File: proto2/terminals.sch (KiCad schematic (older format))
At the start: 111 parts, among them J1 Output 1, J10 Output 6, J11 Device 4, J2 Main Power, J3 Output 2, J4 Output 3, J5 Device 4, J6 Output 4, J7 Device 4, J8 Output 5, J9 Device 4

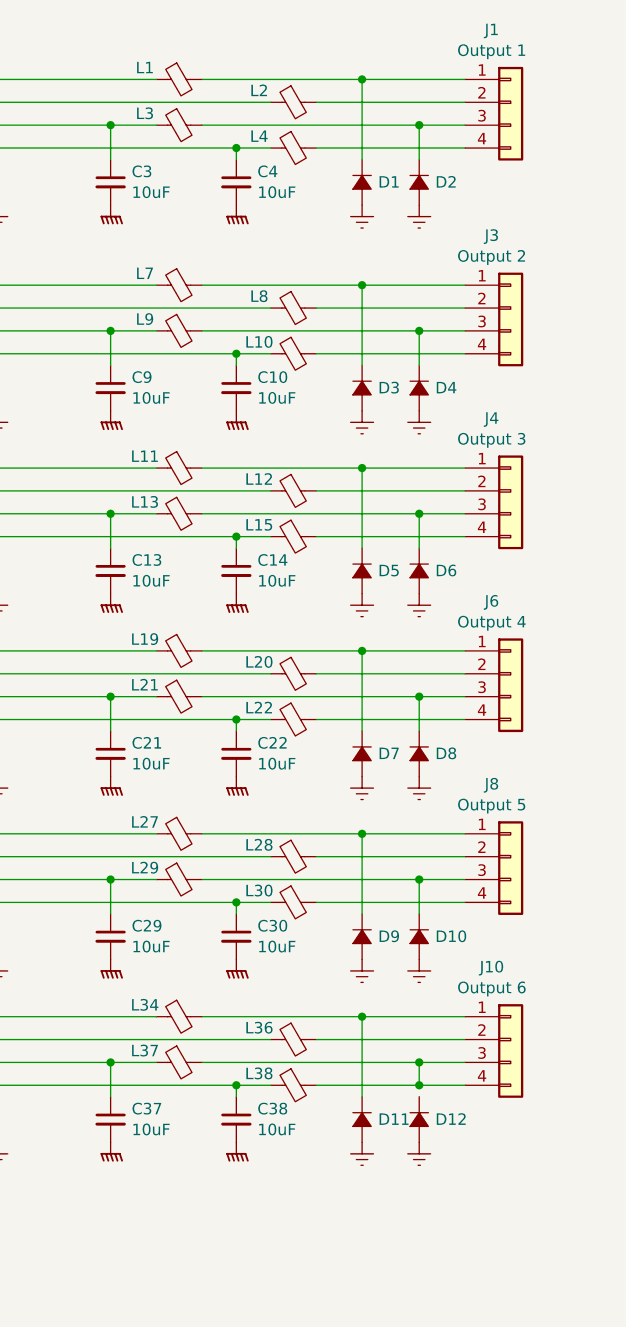
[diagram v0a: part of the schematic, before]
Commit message: Routed Board.
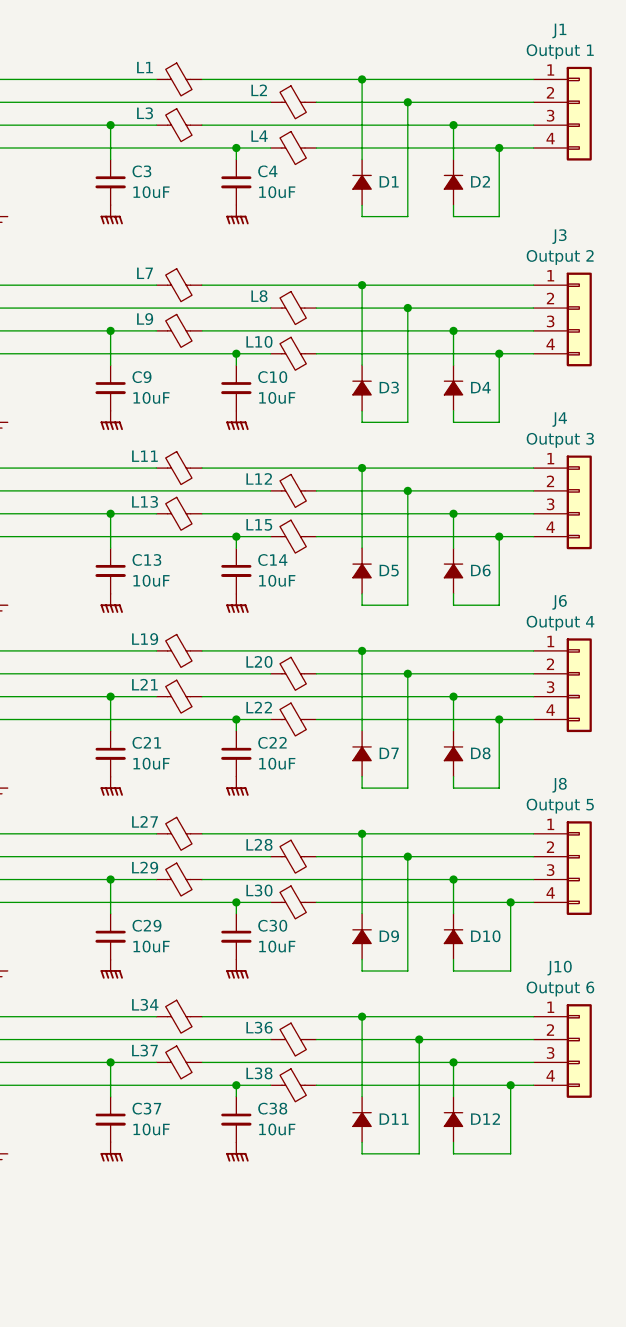
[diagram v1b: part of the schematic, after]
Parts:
- L5, L6: footprint Resistor_SMD:R_1206_3216Metric -> Inductor_BCR:Coilmax_MS0630-2R2M
- MH1, MH2, MH3, MH4: footprint BCR_STD:STD-M6 -> STD-xxx:STD-.125_wide
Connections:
- net Earth: no longer D1.2 (A), D10.2 (A), D11.2 (A), D12.2 (A), D2.2 (A), D3.2 (A), D4.2 (A), D5.2 (A), D6.2 (A), D7.2 (A), D8.2 (A), D9.2 (A)
- net at J1.2 (Pin_2), L2.2: now also D1.2 (A)
- net at J1.4 (Pin_4), L4.2: now also D2.2 (A)
- net at J3.2 (Pin_2), L8.2: now also D3.2 (A)
- net at J3.4 (Pin_4), L10.2: now also D4.2 (A)
- net at J4.2 (Pin_2), L12.2: now also D5.2 (A)
- net at J4.4 (Pin_4), L15.2: now also D6.2 (A)
- net at J6.2 (Pin_2), L20.2: now also D7.2 (A)
- net at J6.4 (Pin_4), L22.2: now also D8.2 (A)
- net at J8.2 (Pin_2), L28.2: now also D9.2 (A)
- net at J8.4 (Pin_4), L30.2: now also D10.2 (A)
- net at J10.2 (Pin_2), L36.2: now also D11.2 (A)
- net at J10.3 (Pin_3), L37.2: now also D12.1 (K); no longer J10.4 (Pin_4), L38.2
- new net: D12.2 (A), J10.4 (Pin_4), L38.2
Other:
- moved on the sheet: D10, D12, D2, D4, D6, D8, J1, J10, J3, J4, J6, J8

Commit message: Finished routing board and other changes, bad commit message, I know.
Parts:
- C1, C10, C11, C12, C13, C14, C15, C16, C17, C18, C19, C2, C20, C21, C22, C23, C24, C25, C26, C27, C28, C29, C3, C30, C31, C32, C33, C34, C35, C36, C37, C38, C39, C4, C40, C41, C42, C7, C8, C9: LCSC (none) -> C440198; LSCS C440198 -> (none)
- C5, C6: LCSC (none) -> C440198
- D1, D10, D11, D12, D2, D3, D4, D5, D6, D7, D8, D9: footprint Diode_SMD:D_0805_2012Metric -> Diode_SMD:D_SOD-123F; LCSC (none) -> C64898; Manufacturer (none) -> MDD; Part Number (none) -> SM4007PL
- J10: value Output 6 -> Output
- J11, J5, J7, J9: value Device 4 -> Device
- J3: value Output 2 -> Output
- J4: value Output 3 -> Output
- J6: value Output 4 -> Output
- J8: value Output 5 -> Output
- L1, L10, L11, L12, L13, L15, L19, L2, L20, L21, L22, L27, L28, L29, L3, L30, L34, L36, L37, L38, L4, L7, L8, L9: value Ferrite_Bead_Small -> 1A Ferrite; LCSC (none) -> C405012
- L14, L16, L17, L18, L23, L24, L25, L26, L31, L32, L33, L35, L39, L40, L41, L42: value Ferrite_Bead_Small -> 500mA Ferrite; LCSC (none) -> C1017
- L5, L6: value 100R 5A -> 100R 5A Ferrite; LCSC (none) -> C380175; Manufacturer (none) -> Coilmax; Part Number (none) -> MS0630-2R2M

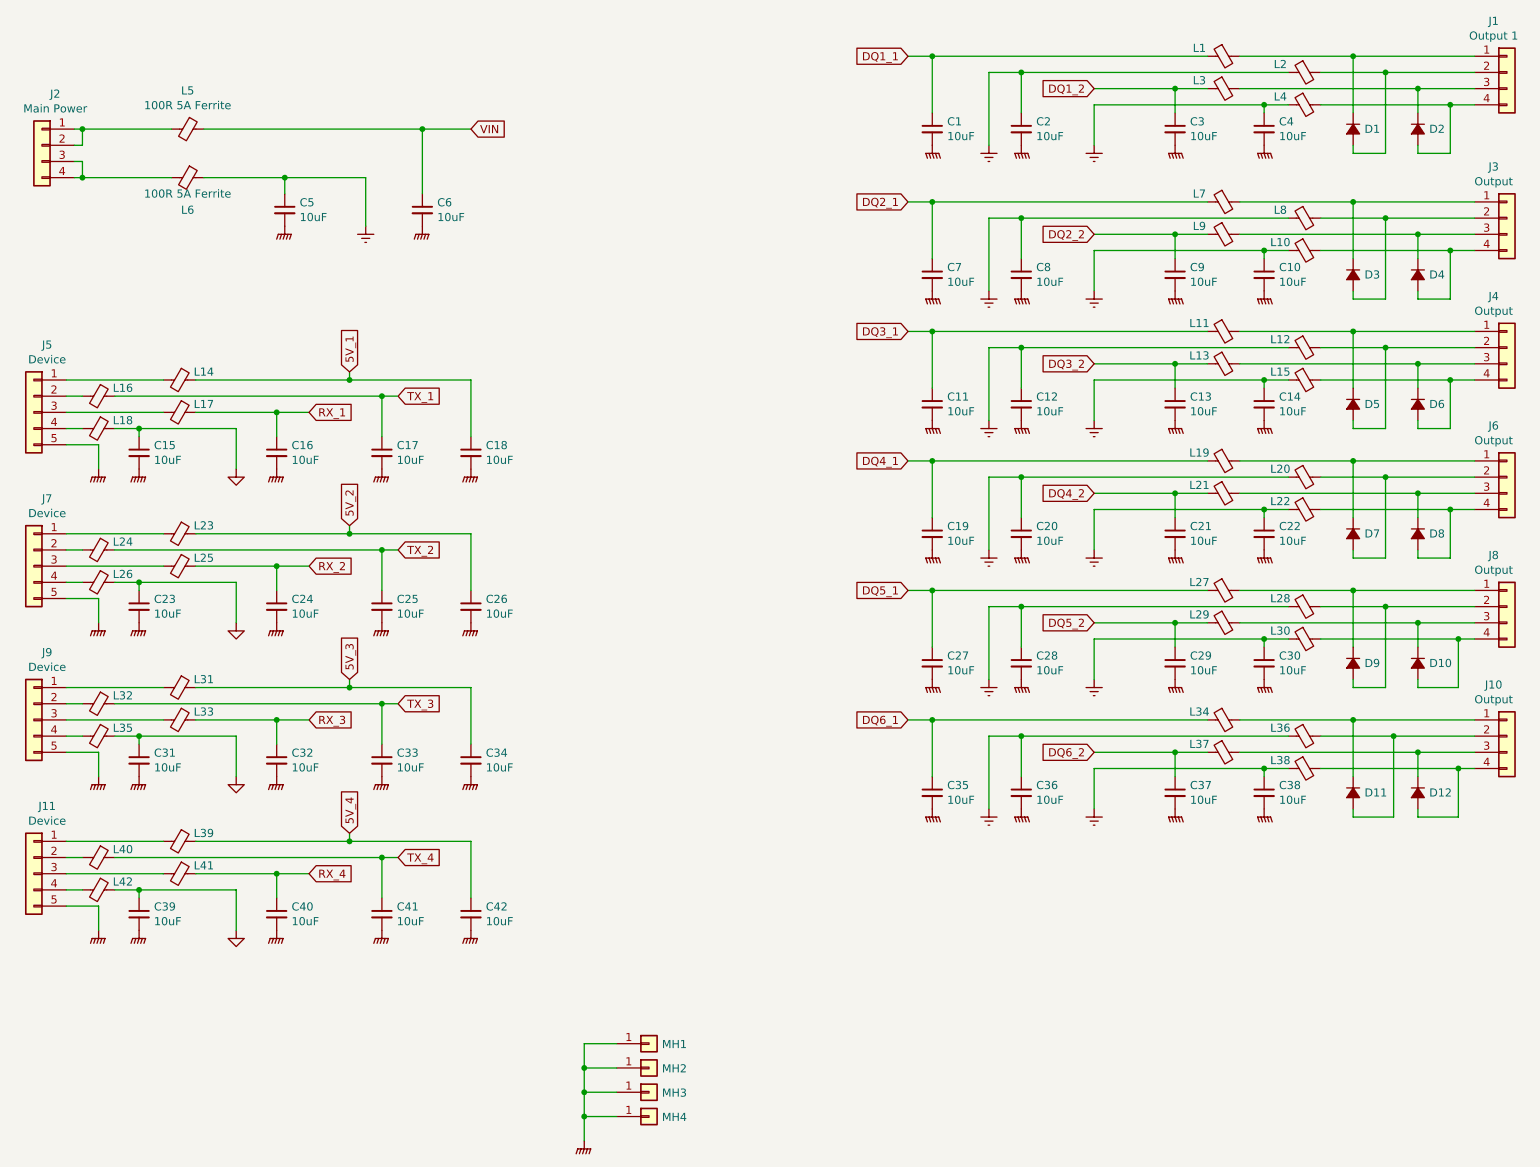
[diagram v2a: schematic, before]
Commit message: Reversed the filter order.
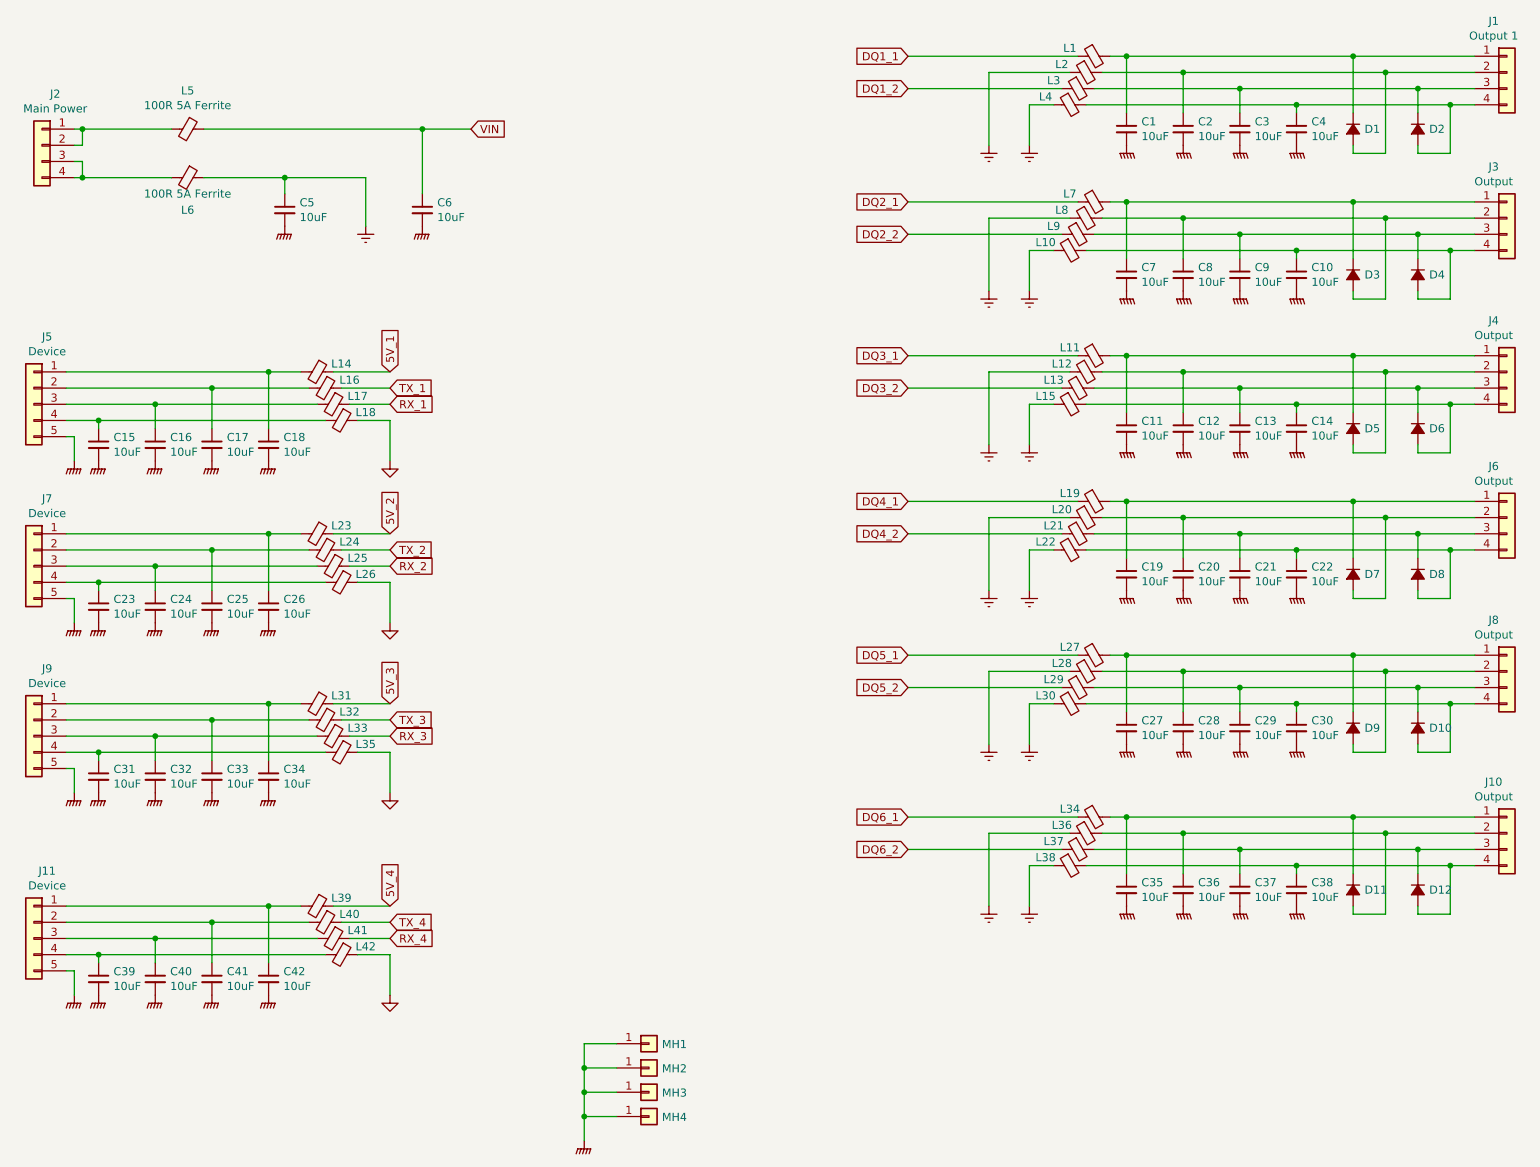
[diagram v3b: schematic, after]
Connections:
- net 5V_1: no longer C18.1
- net 5V_2: no longer C26.1
- net 5V_3: no longer C34.1
- net 5V_4: no longer C42.1
- net DQ1_1: no longer C1.1
- net DQ1_2: no longer C3.1
- net DQ2_1: no longer C7.1
- net DQ2_2: no longer C9.1
- net DQ3_1: no longer C11.1
- net DQ3_2: no longer C13.1
- net DQ4_1: no longer C19.1
- net DQ4_2: no longer C21.1
- net DQ5_1: no longer C27.1
- net DQ5_2: no longer C29.1
- net DQ6_1: no longer C35.1
- net DQ6_2: no longer C37.1
- net Earth: no longer C10.1, C12.1, C14.1, C2.1, C20.1, C22.1, C28.1, C30.1, C36.1, C38.1, C4.1, C8.1
- net GND: no longer C15.1, C23.1, C31.1, C39.1
- net RX_1: no longer C16.1
- net RX_2: no longer C24.1
- net RX_3: no longer C32.1
- net RX_4: no longer C40.1
- net TX_1: no longer C17.1
- net TX_2: no longer C25.1
- net TX_3: no longer C33.1
- net TX_4: no longer C41.1
- net at D1.1 (K), J1.1 (Pin_1), L1.2: now also C1.1
- net at D1.2 (A), J1.2 (Pin_2), L2.2: now also C2.1
- net at D2.1 (K), J1.3 (Pin_3), L3.2: now also C3.1
- net at D2.2 (A), J1.4 (Pin_4), L4.2: now also C4.1
- net at J11.1 (Pin_1), L39.2: now also C42.1
- net at J11.2 (Pin_2), L40.2: now also C41.1
- net at J11.3 (Pin_3), L41.2: now also C40.1
- net at J11.4 (Pin_4), L42.2: now also C39.1
- net at D3.1 (K), J3.1 (Pin_1), L7.2: now also C7.1
- net at D3.2 (A), J3.2 (Pin_2), L8.2: now also C8.1
- net at D4.1 (K), J3.3 (Pin_3), L9.2: now also C9.1
- net at D4.2 (A), J3.4 (Pin_4), L10.2: now also C10.1
- net at D5.1 (K), J4.1 (Pin_1), L11.2: now also C11.1
- net at D5.2 (A), J4.2 (Pin_2), L12.2: now also C12.1
- net at D6.1 (K), J4.3 (Pin_3), L13.2: now also C13.1
- net at D6.2 (A), J4.4 (Pin_4), L15.2: now also C14.1
- net at D7.1 (K), J6.1 (Pin_1), L19.2: now also C19.1
- net at D7.2 (A), J6.2 (Pin_2), L20.2: now also C20.1
- net at D8.1 (K), J6.3 (Pin_3), L21.2: now also C21.1
- net at D8.2 (A), J6.4 (Pin_4), L22.2: now also C22.1
- net at D9.1 (K), J8.1 (Pin_1), L27.2: now also C27.1
- net at D9.2 (A), J8.2 (Pin_2), L28.2: now also C28.1
- net at D10.1 (K), J8.3 (Pin_3), L29.2: now also C29.1
- net at D10.2 (A), J8.4 (Pin_4), L30.2: now also C30.1
- net at D11.1 (K), J10.1 (Pin_1), L34.2: now also C35.1
- net at D11.2 (A), J10.2 (Pin_2), L36.2: now also C36.1
- net at D12.1 (K), J10.3 (Pin_3), L37.2: now also C37.1
- net at D12.2 (A), J10.4 (Pin_4), L38.2: now also C38.1
- net at J9.1 (Pin_1), L31.2: now also C34.1
- net at J9.2 (Pin_2), L32.2: now also C33.1
- net at J9.3 (Pin_3), L33.2: now also C32.1
- net at J9.4 (Pin_4), L35.2: now also C31.1
- net at J7.1 (Pin_1), L23.2: now also C26.1
- net at J7.2 (Pin_2), L24.2: now also C25.1
- net at J7.3 (Pin_3), L25.2: now also C24.1
- net at J7.4 (Pin_4), L26.2: now also C23.1
- net at J5.1 (Pin_1), L14.2: now also C18.1
- net at J5.2 (Pin_2), L16.2: now also C17.1
- net at J5.3 (Pin_3), L17.2: now also C16.1
- net at J5.4 (Pin_4), L18.2: now also C15.1
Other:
- moved on the sheet: C1, C10, C11, C12, C13, C14, C15, C16, C17, C18, C19, C2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
